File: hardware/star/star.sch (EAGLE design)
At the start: 171 parts, among them IC1 MAX481CSA, IC2 LD117AS12TR, IC22 LD117AS12TR, IC3 74HCT08D, IC4 7404D, IC8 MAX481CSA, K1 T90-12VDC-TL-A, K2 T90-12VDC-TL-A, K3 T90-12VDC-TL-A, K5 AQG22110, K6 AQG22110, Q1 35A/25V/8.5mΩ, Q2 35A/25V/8.5mΩ, Q3 35A/25V/8.5mΩ, Q4 35A/25V/8.5mΩ, T1 T_PNP_MMBT5401_CHANGJ_SOT23-B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, T2 T_PNP_MMBT5401_CHANGJ_SOT23-B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, T3 T_PNP_MMBT5401_CHANGJ_SOT23-B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, T4 T_PNP_MMBT5401_CHANGJ_SOT23-B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, U1 TCLT1600

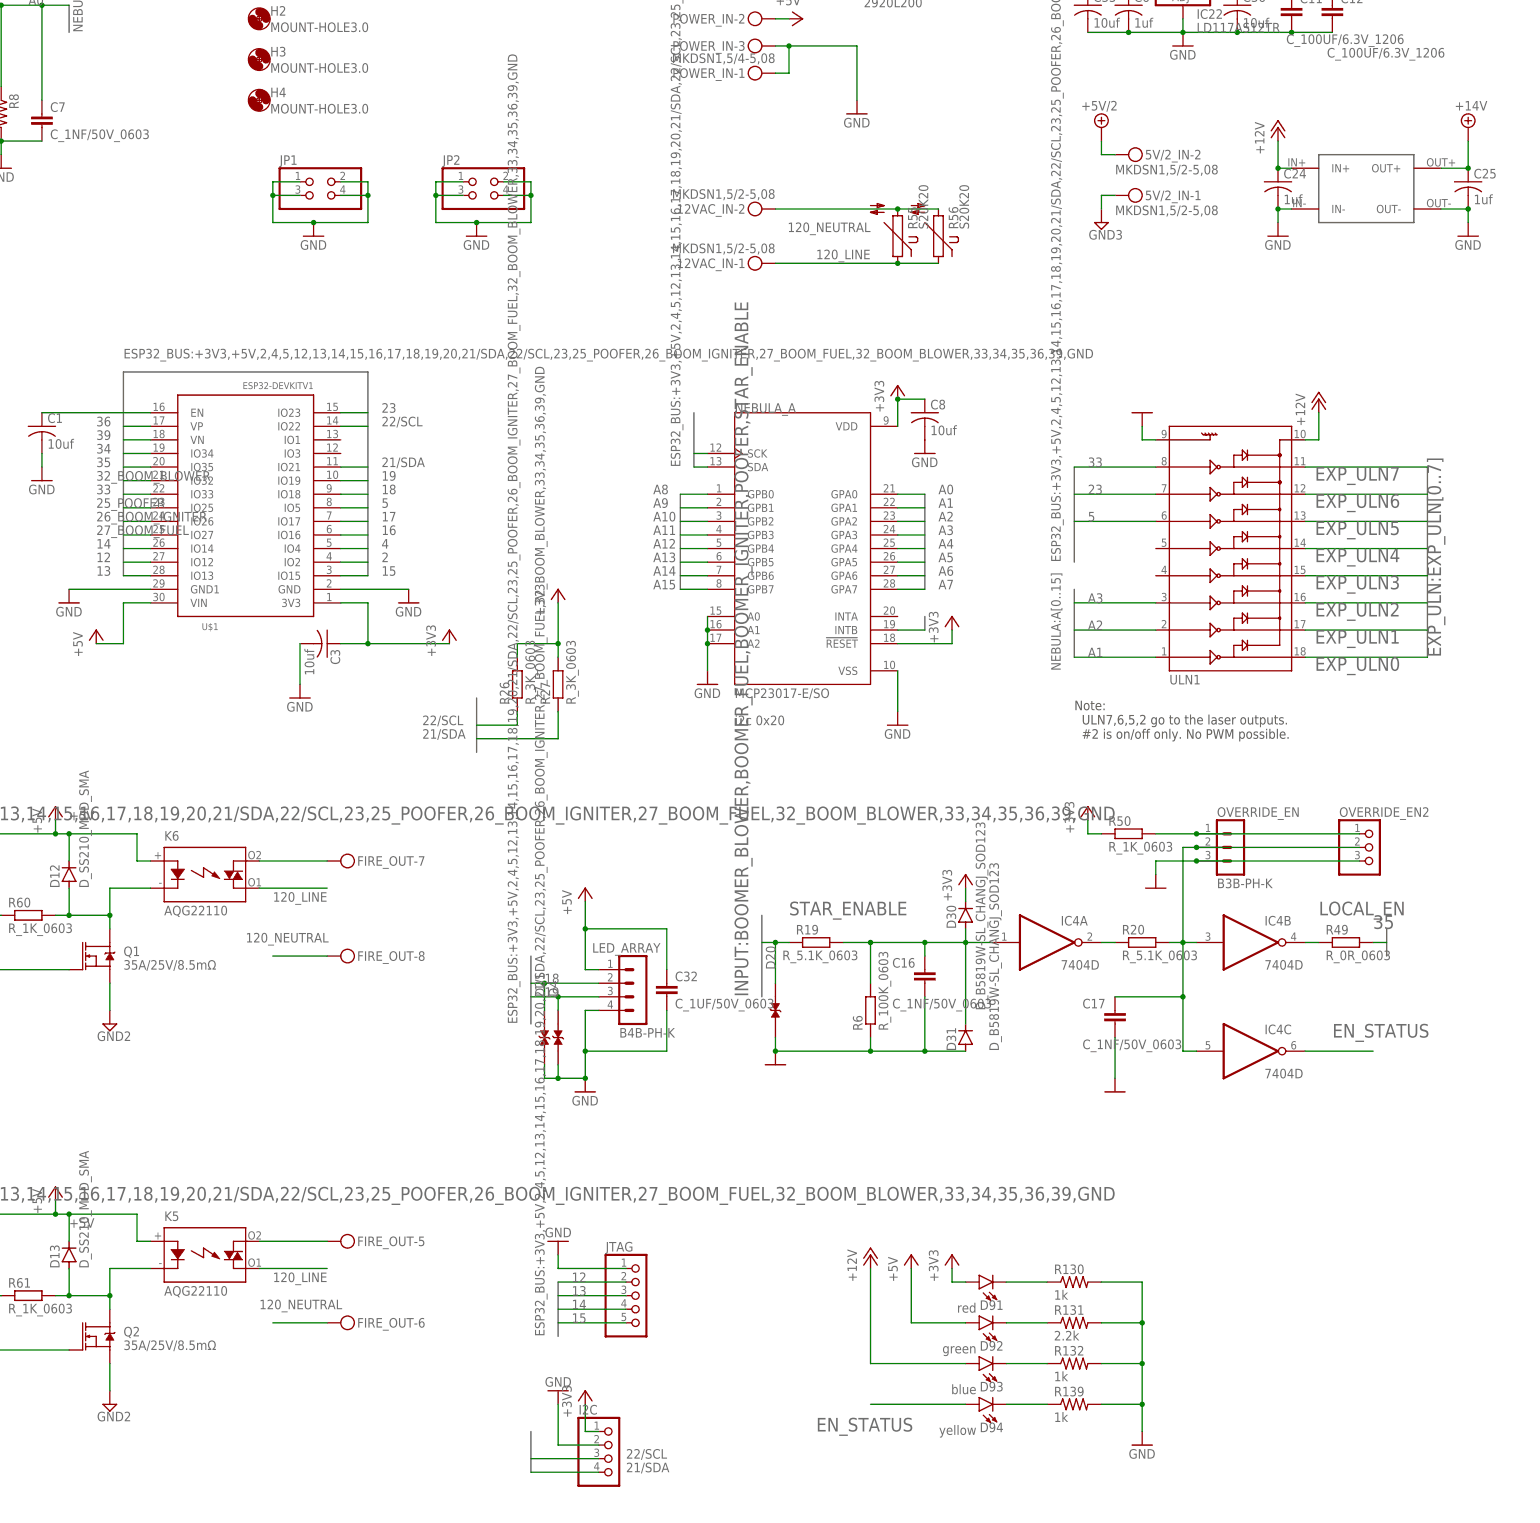
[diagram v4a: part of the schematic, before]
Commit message: Added switching 5v regulator
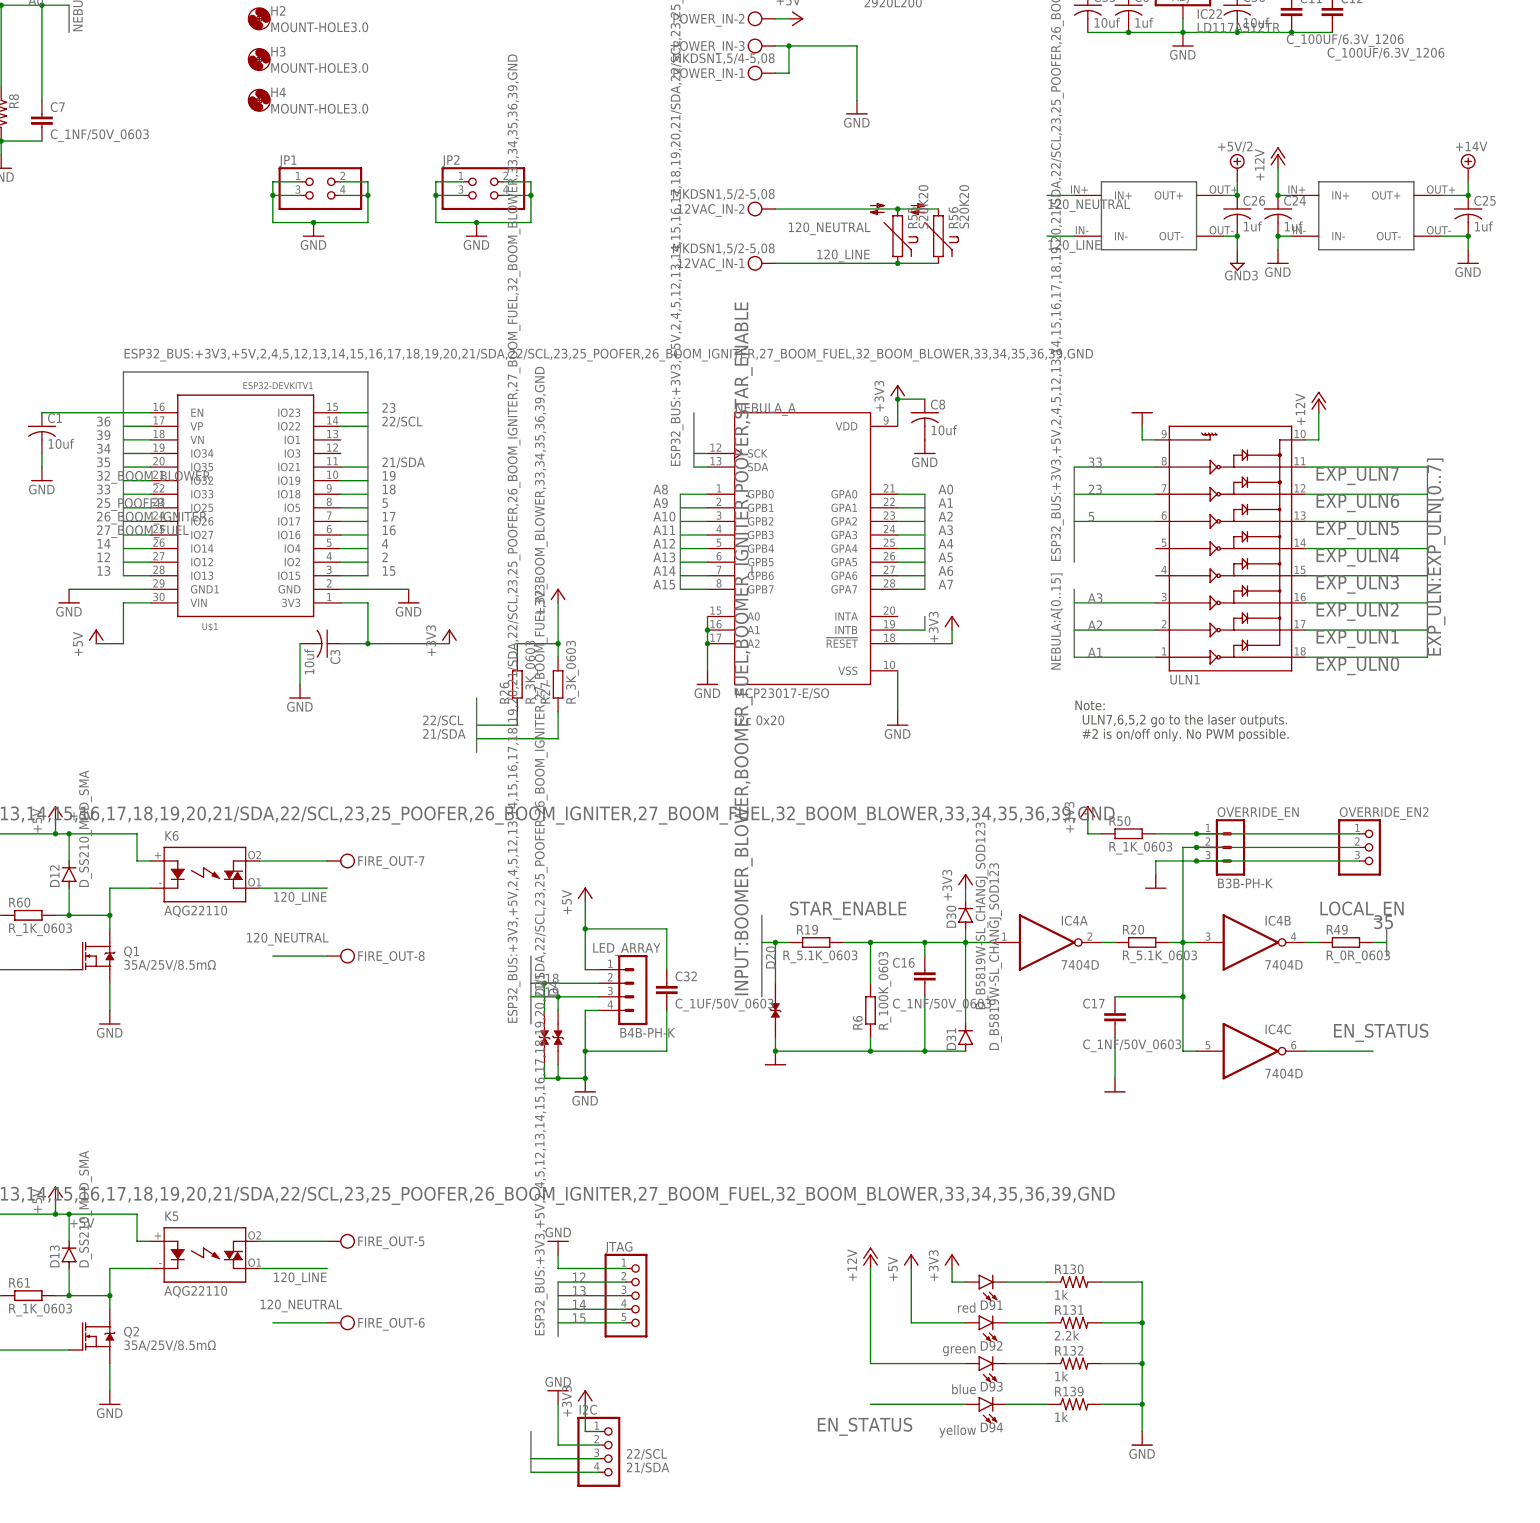
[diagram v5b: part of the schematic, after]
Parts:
- removed 5V/2_IN: MKDSN1,5/2-5,08, con-phoenix-508-jm:MKDSN1,5/2-5,08
- added C26: 1uf, rcl:C-USC0805
- added U$3: EPS-25, Nova:EPS-25
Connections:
- removed net GND2: Q1.S, Q2.S
- net +5V/2: now also C26.1, U$3.OUT+; no longer 5V/2_IN-2.KL
- net 120_LINE: now also U$3.IN-
- net 120_NEUTRAL: now also U$3.IN+
- net GND: now also Q1.S, Q2.S
- net GND3: now also C26.2, U$3.OUT-; no longer 5V/2_IN-1.KL
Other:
- moved on the sheet: C24, C25

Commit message: Lots of updates
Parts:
- removed C10, C9: C_100UF/6.3V_1206, JLC PCB Basic Parts_loc:C_100UF/6.3V_1206
- removed C2, C5: 10uf, rcl:C-USC0603
- removed C24, C26, C4: 1uf, rcl:C-USC0805
- removed F2: 2920L200, 2920L200:2920L200
- removed JP2: (no value), pinhead:PINHD-2X2
- removed U$2: ZK-SJVA-4X, Nova:ZK-SJVA-4X
- removed U$3: EPS-25, Nova:EPS-25
- added EPP-120S-24: EPP-120S, Nova:EPP-120S
- added NID35-12, NID35-5: NID35, Nova:NID35
- added SKA15B-05: SKA15B, Nova:SKA15B
- IC2: value LD117AS12TR -> 74HCT08D; device v-reg:LD117AS12TR -> 74xx-eu:74HCT08D; LCSC_PART C6187 -> C5593; PRICE 0.5 -> (none)
- R62: value R_7.5K_0603 -> R_15K_0603; device JLC PCB Basic Parts_loc:R_7.5K_0603 -> JLC PCB Basic Parts_loc:R_15K_0603
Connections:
- removed net +14V: C25.1, D14.C, D17.A, FIRE_OUT-3.KL, U$2.OUT+
- removed net N$59: F2.1, POWER_IN-4.KL
- new net +24V: C25.1, D14.C, D17.A, EPP-120S-24.OUT+, FIRE_OUT-3.KL, NID35-12.IN1, NID35-12.IN2, NID35-5.IN1, NID35-5.IN2, SKA15B-05.IN+
- new net N$60: IC2A.O, Q4.G
- net +12V: now also NID35-12.OUT1, NID35-12.OUT2, NID35-12.OUT3, NID35-12.OUT4, POWER_IN-4.KL; no longer C2.1, C24.1, C28.+, C35.1, C4.1, C6.1, C89.+, F2.2, IC2.IN, IC22.IN, U$2.IN+
- net +3V3: now also C28.+, IC2P.VCC
- net +5V: now also C35.1, C6.1, C89.+, IC22.IN, NID35-5.OUT1, NID35-5.OUT2, NID35-5.OUT3, NID35-5.OUT4; no longer C10.1, C5.1, C9.1, IC2.OUT
- net +5V/2: now also SKA15B-05.OUT+; no longer C26.1, U$3.OUT+
- net 120_LINE: now also EPP-120S-24.IN-; no longer U$3.IN-
- net 120_NEUTRAL: now also EPP-120S-24.IN+; no longer U$3.IN+
- net 15: now also IC2A.I1
- net 26_BOOM_IGNITER: now also IC2A.I0; no longer Q4.G
- net GND: now also EPP-120S-24.OUT-, IC2P.GND, NID35-12.COM1, NID35-12.COM2, NID35-5.COM1, NID35-5.COM2, SKA15B-05.IN-; no longer C10.2, C2.2, C24.2, C4.2, C5.2, C9.2, IC2.ADJ, JP2.1, JP2.2, JP2.3, JP2.4, U$2.IN-, U$2.OUT-
- net GND3: now also SKA15B-05.OUT-; no longer C26.2, U$3.OUT-
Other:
- moved on the sheet: C11, C12, C25, C28, C35, C36, C6, C89, IC22

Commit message: Manual routing complete
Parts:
- added X1: MKDSN1,5/2-5,08, con-phoenix-508-jm:MKDSN1,5/2-5,08
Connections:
- net +24V: now also X1-2.KL
- net 26_BOOM_IGNITER: now also Q4.G; no longer IC2A.I0
- net 32_BOOM_BLOWER: now also IC2A.I0; no longer Q3.G
- net GND: now also X1-1.KL
- net N$60: now also Q3.G; no longer Q4.G
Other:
- moved on the sheet: D14, D17, FIRE_OUT-3, FIRE_OUT-4, IC2A, IC2P, POWER_IN-1, POWER_IN-2, POWER_IN-3, POWER_IN-4, Q3, R62

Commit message: swap to schmitt trigger
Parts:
- removed R15, R24, R33, R40: R_10R_0603, JLC PCB Basic Parts_loc:R_10R_0603
- removed R17, R28, R35, R42: R_2.7K_0603, JLC PCB Basic Parts_loc:R_2.7K_0603
- removed R18, R29, R36, R43: R_1K_0603, JLC PCB Basic Parts_loc:R_1K_0603
- removed T1, T2, T3, T4: T_PNP_MMBT5401_CHANGJ_SOT23-BEC, JLC PCB Basic Parts_loc:T_PNP_MMBT5401_CHANGJ_SOT23-BEC
- added C2, C4: C_1UF/50V_0603, JLC PCB Basic Parts_loc:C_1UF/50V_0603
- added H5, H6: MOUNT-HOLE4.1, holes:MOUNT-HOLE4.1
- added U2: ADXL343BCCZ-RL7, ADXL343BCCZ-RL7:ADXL343BCCZ-RL7
- added U3: TMP102AIDRLR, TMP102AIDRLR:TMP102AIDRLR
- added U4, U5, U6, U7: SN74LVC1G17DCK, SN74LVC1G17:SN74LVC1G17DCK
- R16, R25, R34, R41: value R_12K_0603 -> R_1K_0603; device JLC PCB Basic Parts_loc:R_12K_0603 -> JLC PCB Basic Parts_loc:R_1K_0603
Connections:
- removed net N$19: IC3A.I0, R17.1, R18.2
- removed net N$20: R15.1, T1.E
- removed net N$28: IC3B.I0, R28.1, R29.2
- removed net N$29: R24.1, T2.E
- removed net N$34: IC3C.I0, R35.1, R36.2
- removed net N$35: R33.1, T3.E
- removed net N$40: IC3D.I0, R42.1, R43.2
- removed net N$41: R40.1, T4.E
- net +12V: no longer R15.2, R24.2, R33.2, R40.2
- net +3V3: now also C2.1, C4.1, U2.!CS, U2.SDO/ALT_ADDRESS, U2.VDDIO, U2.VS, U3.V+, U4.VCC, U5.VCC, U6.VCC, U7.VCC
- net 21/SDA: now also U2.SDA/SDI/SDIO, U3.SDA
- net 22/SCL: now also U2.SCL/SCLK, U3.SCL
- net GND: now also C2.2, C4.2, U2.GND, U3.ADD0, U3.GND, U4.GND, U5.GND, U6.GND, U7.GND; no longer R18.1, R29.1, R36.1, R43.1
- net N$16: now also IC3A.I0, U4.Y; no longer R17.2, T1.C
- net N$17: now also U4.A; no longer T1.B
- net N$25: now also U7.A; no longer T2.B
- net N$26: now also IC3B.I0, U7.Y; no longer R28.2, T2.C
- net N$31: now also U5.A; no longer T3.B
- net N$32: now also IC3C.I0, U5.Y; no longer R35.2, T3.C
- net N$37: now also U6.A; no longer T4.B
- net N$38: now also IC3D.I0, U6.Y; no longer R42.2, T4.C
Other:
- moved on the sheet: 5V_CTRL_LAZERS, C16, C17, C32, C33, D12, D13, D14, D15, D16, D17, D18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
